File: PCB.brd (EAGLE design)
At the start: 28.6 x 50.8 mm, 22 parts

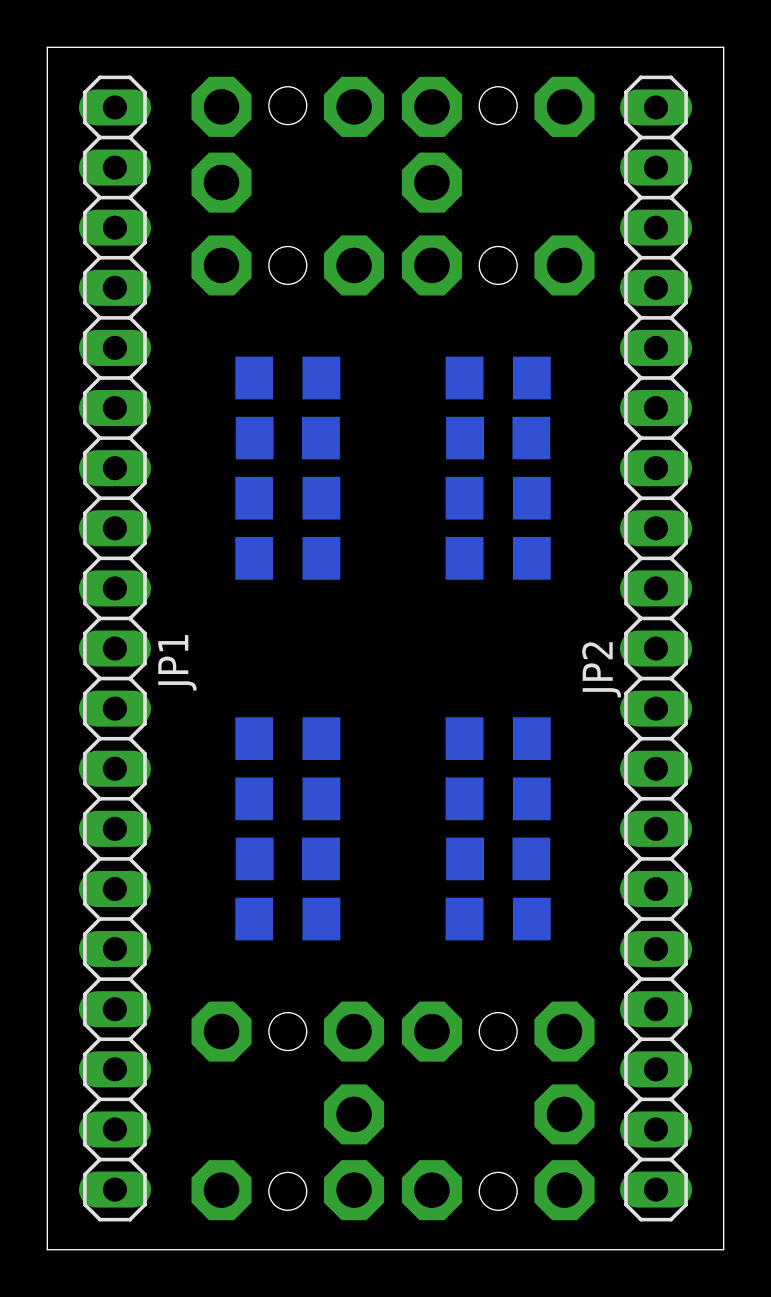
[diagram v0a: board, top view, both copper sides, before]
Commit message: Revision A. Only 4 jacks can be nested between pins of ESP32 so design changed to accept only 4.
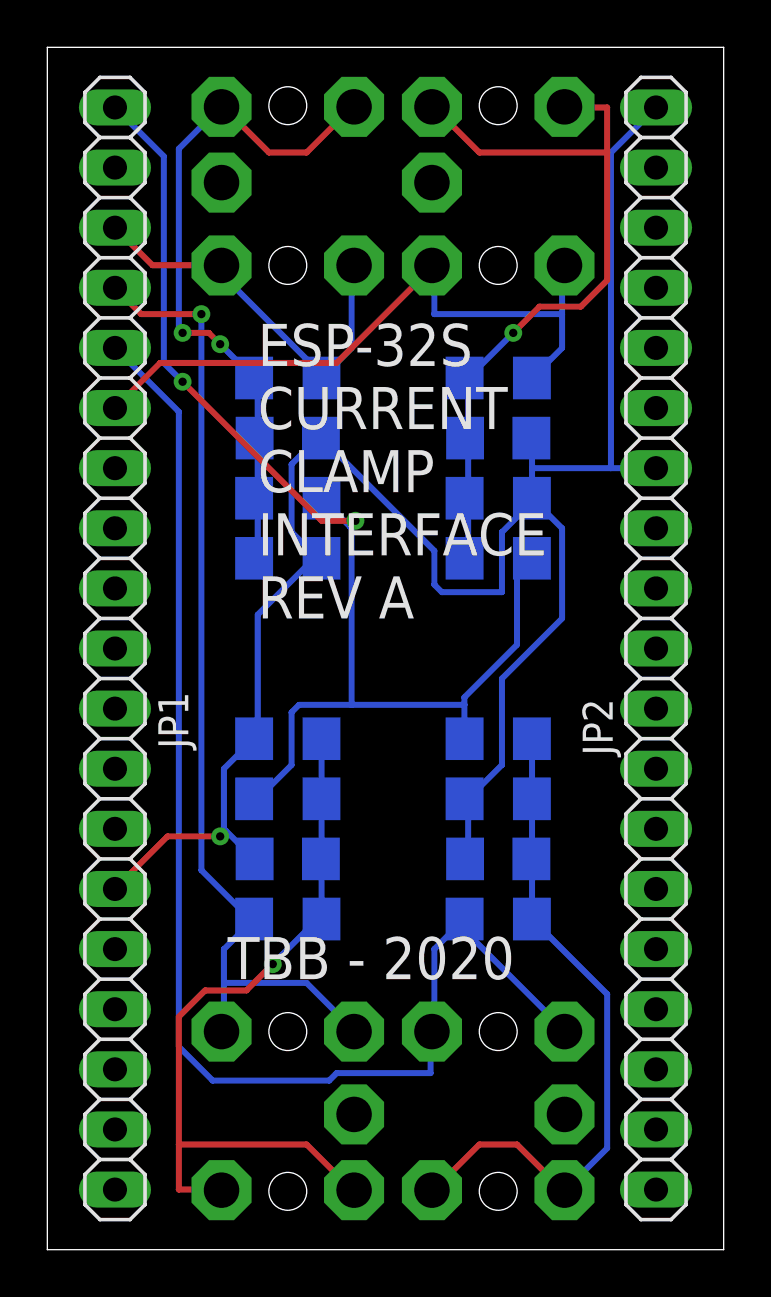
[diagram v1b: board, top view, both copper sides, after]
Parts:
- turned C4 to 180 degrees
- turned R10 to 180 degrees
- turned R11 to 180 degrees
- turned R2 to 180 degrees
- turned R6 to 180 degrees
- turned R9 to 180 degrees
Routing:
- net GND: track 0.00 -> 84.4 mm, vias 0 -> 1
- net ADC_GPIO34: track 0.00 -> 55.7 mm
- net +3V3: track 0.00 -> 52.8 mm, vias 0 -> 2
- net ADC_GPIO39: track 0.00 -> 42.4 mm, vias 0 -> 1
- net N$7: track 0.00 -> 33.1 mm, vias 0 -> 1
- net N$1: track 0.00 -> 32.7 mm, vias 0 -> 1
- net N$2: track 0.00 -> 29.6 mm, vias 0 -> 2
- net ADC_GPIO35: track 0.00 -> 28.7 mm
- net N$5: track 0.00 -> 28.4 mm
- net ADC_GPIO36: track 0.00 -> 17.0 mm
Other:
- board text added: "CL0"
- board text added: "CL1"
- board text added: "CL2"
- board text added: "CL3"
- board text added: "ESP-32S CURRENT CLAMP INTERFACE REV A"
- board text added: "GPIO34"
- board text added: "GPIO35"
- board text added: "GPIO36"
- board text added: "GPIO39"
- board text added: "TBB - 2020"
